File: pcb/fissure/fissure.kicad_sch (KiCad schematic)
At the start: 64 parts, among them J1 Conn_01x04_Female, J2 USB_C_Receptacle_USB2.0, J3 Conn_01x06, J4 Conn_01x06, J5 OLED, J6 Conn_01x06, J7 Conn_01x06, K1 KEY, K10 KEY, K11 KEY, K12 KEY, K13 KEY, K14 KEY, K15 KEY, K16 KEY, K17 KEY, K18 KEY, K19 KEY, K2 KEY, K20 KEY, K3 KEY, K4 KEY, K5 KEY, K6 KEY, K7 KEY, K8 KEY, K9 KEY, Q1 AO3401A, Q2 AO3401A, SW1 SW_Push, SW2 SW_Push, SW3 SW_SPDT, SW4 SW_SPDT, U1 Holyiot_18010, U2 MT25QL128ABA1ESE, U3 LTC4054ES5-4.2, U4 MCP1700-3302E_SOT23

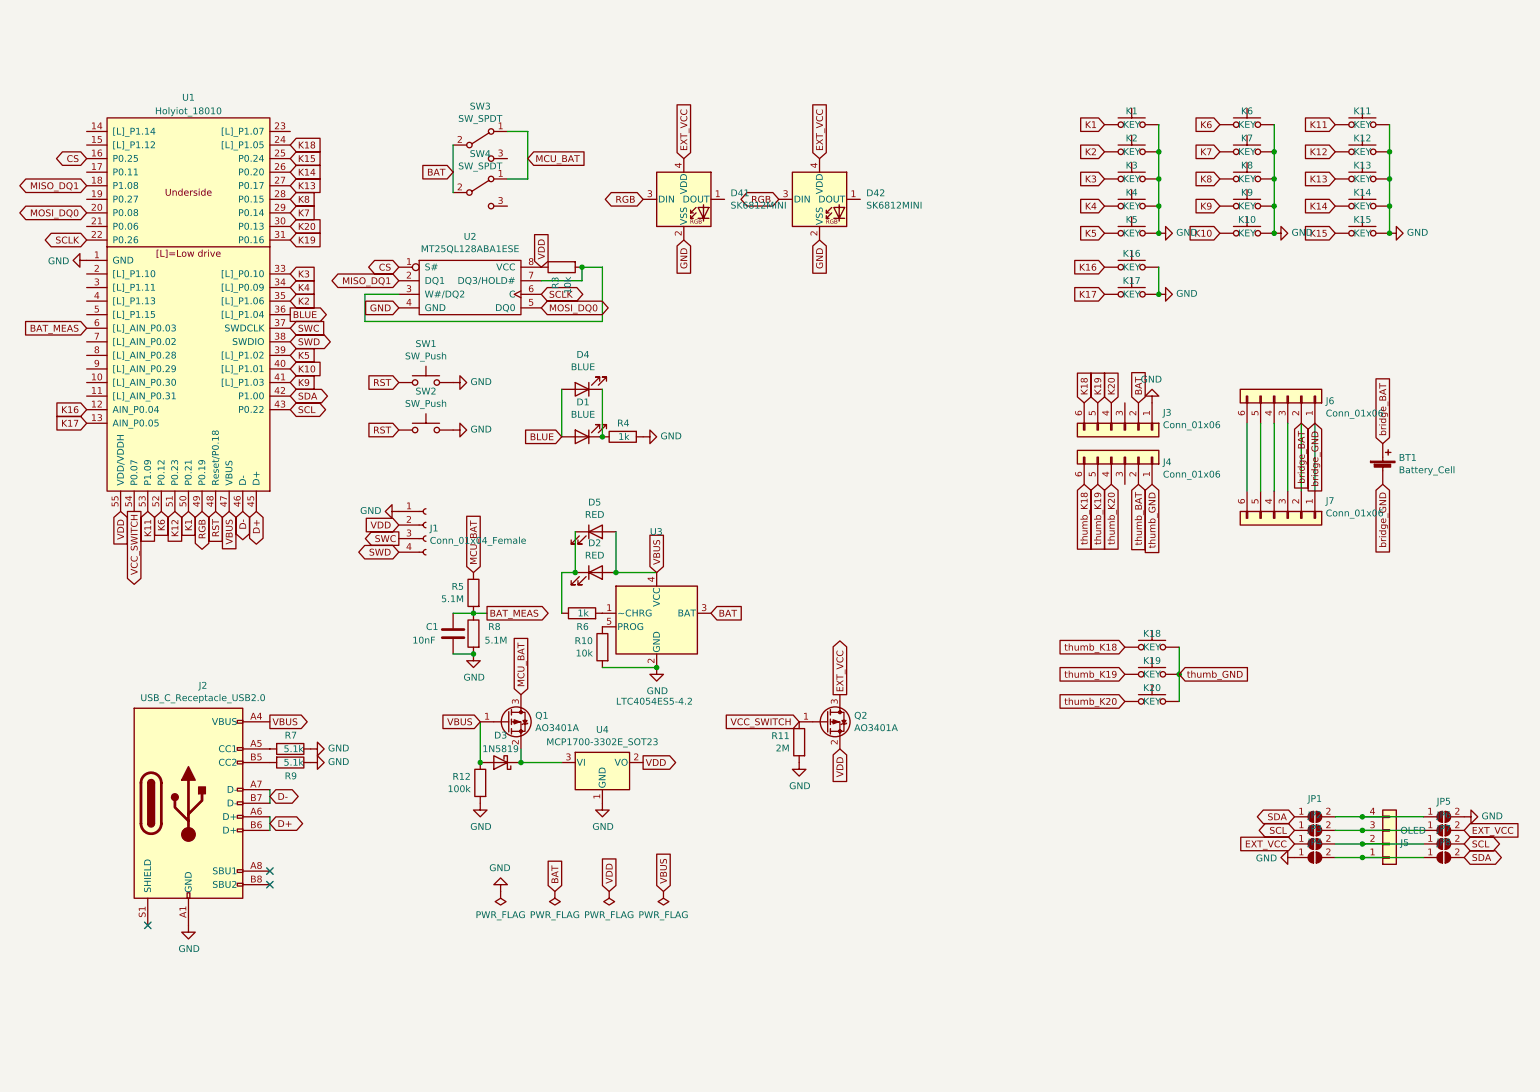
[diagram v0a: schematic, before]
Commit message: stagger update
- middle 2 mm up
- outer index flat with home
- narrower pinky columns
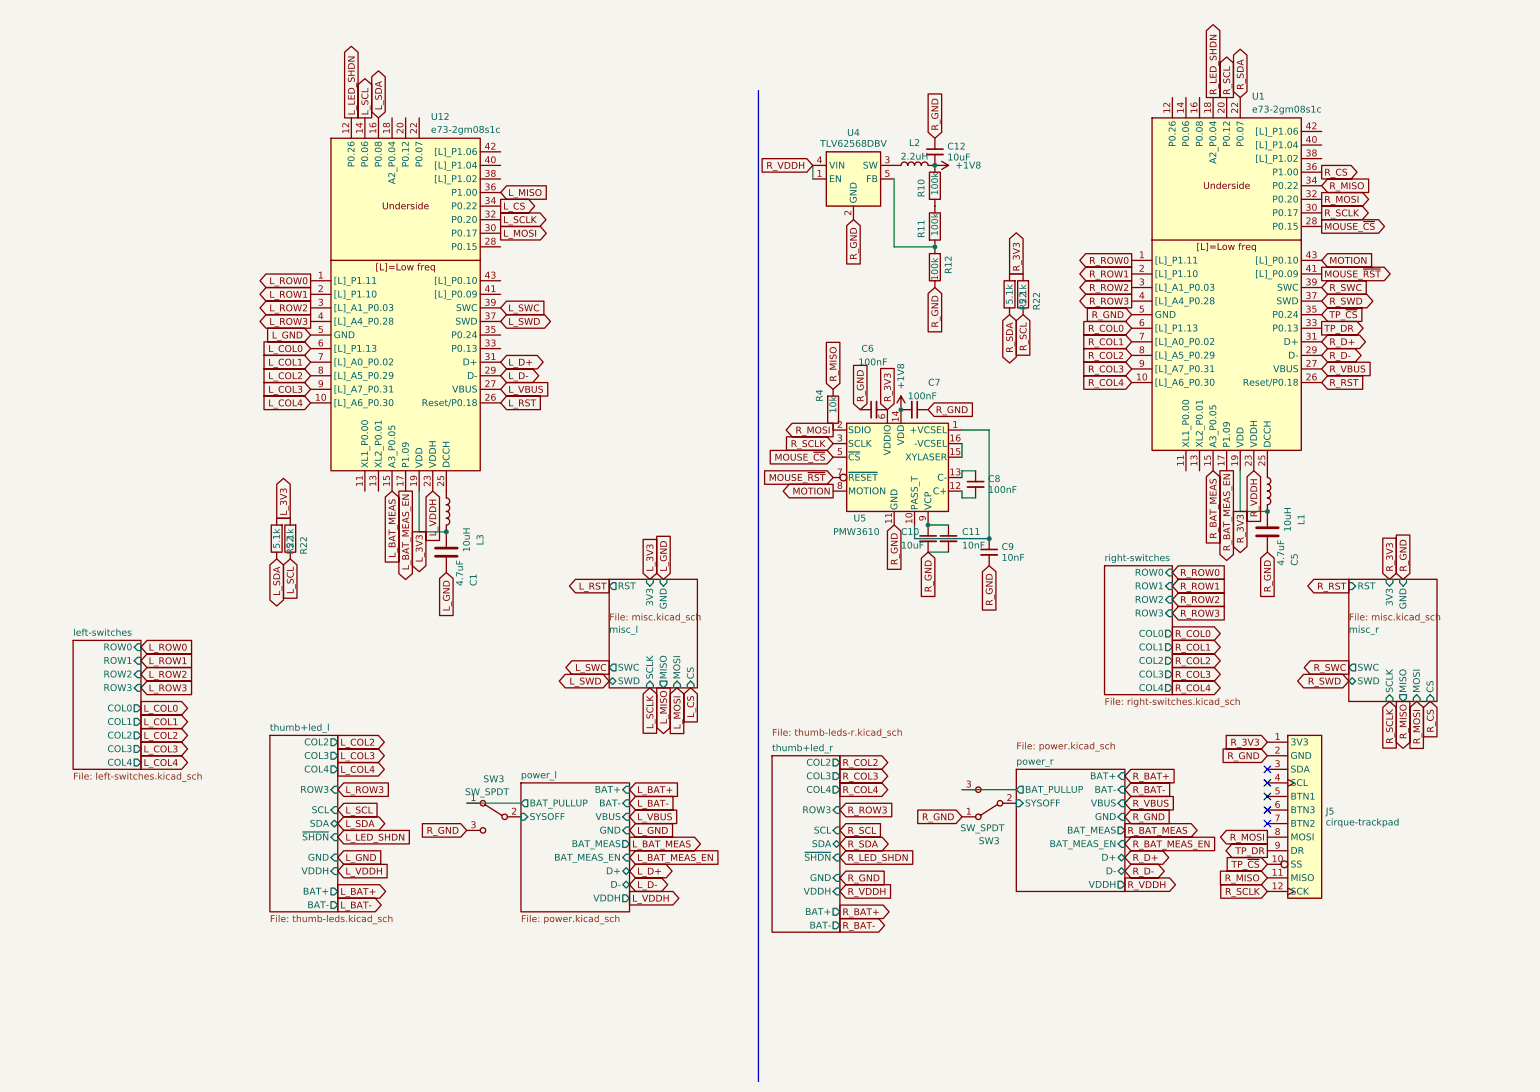
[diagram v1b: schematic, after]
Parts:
- removed BT1: Battery_Cell, misc:BA1AAAPC, symbol Device:Battery_Cell
- removed D1, D4: BLUE, LED_SMD:LED_1206_3216Metric, symbol Device:LED
- removed D2, D5: RED, LED_SMD:LED_1206_3216Metric, symbol Device:LED
- removed D3: 1N5819, Diode_SMD:D_SOD-323, symbol Diode:1N5819
- removed D41, D42: SK6812MINI, LED_SMD:LED_SK6812MINI_PLCC4_3.5x3.5mm_P1.75mm, symbol LED:SK6812MINI
- removed J1: Conn_01x04_Female, fissure:debug-port, symbol Connector:Conn_01x04_Female
- removed J2: USB_C_Receptacle_USB2.0, Connector_USB:USB_C_Receptacle_HRO_TYPE-C-31-M-12, symbol Connector:USB_C_Receptacle_USB2.0
- removed J3, J4: Conn_01x06, fissure:bridge-conn, symbol Connector_Generic:Conn_01x06
- removed J5: OLED, misc:OLED, symbol Connector_Generic:Conn_01x04
- removed J6, J7: Conn_01x06, fissure:bridge, symbol Connector_Generic:Conn_01x06
- removed JP1, JP2, JP3, JP4, JP5, JP6, JP7, JP8: SolderJumper_2_Open, Jumper:SolderJumper-2_P1.3mm_Open_RoundedPad1.0x1.5mm, symbol Jumper:SolderJumper_2_Open
- removed K1, K11, K12, K13, K16, K17, K18, K19, K2, K20, K3, K6, K7, K8: KEY, pg1350:PG1350-reversible-no-diode-short, symbol Switch:SW_Push
- removed K10, K15, K5: KEY, pg1350:PG1350-reversible-no-diode-short-offcenter-outer, symbol Switch:SW_Push
- removed K14, K4, K9: KEY, pg1350:PG1350-reversible-no-diode-short-offcenter, symbol Switch:SW_Push
- removed Q1, Q2: AO3401A, Package_TO_SOT_SMD:SOT-23, symbol Transistor_FET:AO3401A
- removed R3: 10k, Resistor_SMD:R_0805_2012Metric, symbol Device:R
- removed R5, R8: 5.1M, Resistor_SMD:R_0603_1608Metric, symbol Device:R
- removed R6: 1k, Resistor_SMD:R_0603_1608Metric, symbol Device:R
- removed R7, R9: 5.1k, Resistor_SMD:R_0603_1608Metric, symbol Device:R
- removed SW1, SW2: SW_Push, Button_Switch_SMD:SW_SPST_B3U-1000P, symbol Switch:SW_Push
- removed SW3, SW4: SW_SPDT, Button_Switch_SMD:SW_SPDT_PCM12, symbol Switch:SW_SPDT
- removed U1: Holyiot_18010, misc:Holyiot_18010, symbol holyiot_18010:Holyiot_18010
- removed U2: MT25QL128ABA1ESE, Package_SO:SOP-8_5.28x5.23mm_P1.27mm, symbol steno:MT25QL128ABA1ESE
- removed U3: LTC4054ES5-4.2, Package_TO_SOT_SMD:TSOT-23-5, symbol Battery_Management:LTC4054ES5-4.2
- removed U4: MCP1700-3302E_SOT23, Package_TO_SOT_SMD:SOT-23, symbol Regulator_Linear:MCP1700-3302E_SOT23
- added C10, C12: 10uF, Capacitor_SMD:C_0603_1608Metric, symbol Device:C_Small
- added C11, C9: 10nF, Capacitor_SMD:C_0603_1608Metric, symbol Device:C_Small
- added C5: 4.7uF, Capacitor_SMD:C_0603_1608Metric, symbol Device:C
- added C6, C7, C8: 100nF, Capacitor_SMD:C_0603_1608Metric, symbol Device:C_Small
- added J5: cirque-trackpad, Connector_FFC-FPC:Hirose_FH12-12S-0.5SH_1x12-1MP_P0.50mm_Horizontal, symbol misc:cirque-trackpad
- added L1, L3: 10uH, Inductor_SMD:L_0603_1608Metric, symbol Device:L
- added L2: 2.2uH, Inductor_SMD:L_1008_2520Metric, symbol Device:L
- added R22 (x4): 5.1k, Resistor_SMD:R_0603_1608Metric, symbol Device:R
- added SW3 (x2): SW_SPDT, Button_Switch_SMD:SW_SPDT_PCM12, symbol Switch:SW_SPDT
- added U1, U12: e73-2gm08s1c, mcu:e73-2g4m08s1c-shrunk, symbol mcu:e73-2gm08s1c
- added U4: TLV62568DBV, Package_TO_SOT_SMD:SOT-23-5, symbol Regulator_Switching:TLV62568DBV
- added U5: PMW3610, sensor:PMW3610, symbol sensor:PMW3610
- C1: value 10nF -> 4.7uF
- R10: value 10k -> 100k
- R11: value 2M -> 100k
- R4: value 1k -> 10k
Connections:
- net VBUS is gone; now on net GND: R12.1
- net GND: now also C10.2, C11.2, C12.1, C5.2, C6.1, C7.1, C9.2, J5.2 (GND), SW3.1 (A), SW3.3 (C), U1.21 (GND), U1.24 (GND), U1.5 (GND), U12.21 (GND), U12.24 (GND), U12.5 (GND), U4.2 (GND), U5.11 (GND); no longer R10.2, R11.2, R12.2, R4.2
- net R_MOSI: now reaches R4.1
- net R_MOSI: now also J5.8 (MOSI), U1.32 (P0.20), U5.2 (SDIO)
- net +1V8: now reaches R10.1
- net +1V8: now also C12.2, C7.2, L2.2, U5.14 (VDD)
- net BAT_MEAS renamed L_3V3
- net L_3V3: now also L3.2, R22.2, R22.2, U12.19 (VDD)
- net VCC_SWITCH: no longer names the net of R11.1
- net VCC_SWITCH: now also R10.2
- new net: L1.1, U1.25 (DCCH)
- new net: R11.2, R12.2, U4.5 (FB)
- new net: L3.1, U12.25 (DCCH)
- new net: C10.1, C11.1, U5.9 (VCP)
- new net: C9.1, U5.1 (+VCSEL), U5.10 (PASS_T)
- new net: C8.2, U5.12 (C+)
- new net: C8.1, U5.13 (C-)
- new net: U5.15 (XYLASER), U5.16 (-VCSEL)
- new net: L2.1, U4.3 (SW)
- new net L_BAT_MEAS: U12.15 (A3_P0.05)
- new net L_BAT_MEAS_EN: U12.17 (P1.09)
- new net L_COL0: U12.6 ([L]_P1.13)
- new net L_COL1: U12.7 ([L]_A0_P0.02)
- new net L_COL2: U12.8 ([L]_A5_P0.29)
- new net L_COL3: U12.9 ([L]_A7_P0.31)
- new net L_COL4: U12.10 ([L]_A6_P0.30)
- new net L_CS: U12.34 (P0.22)
- new net L_D+: U12.31 (D+)
- new net L_D-: U12.29 (D-)
- new net L_LED_SHDN: U12.12 (P0.26)
- new net L_MISO: U12.36 (P1.00)
- new net L_MOSI: U12.30 (P0.17)
- new net L_ROW0: U12.1 ([L]_P1.11)
- new net L_ROW1: U12.2 ([L]_P1.10)
- new net L_ROW2: U12.3 ([L]_A1_P0.03)
- new net L_ROW3: U12.4 ([L]_A4_P0.28)
- new net L_RST: U12.26 (Reset/P0.18)
- new net L_SCL: R22.1, U12.14 (P0.06)
- new net L_SCLK: U12.32 (P0.20)
- new net L_SDA: R22.1, U12.16 (P0.08)
- new net L_SWC: U12.39 (SWC)
- new net L_SWD: U12.37 (SWD)
- new net L_VBUS: U12.27 (VBUS)
- new net L_VDDH: U12.23 (VDDH)
- new net MOTION: U1.43 ([L]_P0.10), U5.8 (MOTION)
- new net MOUSE_~{CS}: U1.28 (P0.15), U5.5 (~{CS})
- new net MOUSE_~{RST}: U1.41 ([L]_P0.09), U5.7 (~{RESET})
- new net R_3V3: C5.1, C6.2, J5.1 (3V3), L1.2, R22.2, R22.2, U1.19 (VDD), U5.6 (VDDIO)
- new net R_BAT_MEAS: U1.15 (A3_P0.05)
- new net R_BAT_MEAS_EN: U1.17 (P1.09)
- new net R_COL0: U1.6 ([L]_P1.13)
- new net R_COL1: U1.7 ([L]_A0_P0.02)
- new net R_COL2: U1.8 ([L]_A5_P0.29)
- new net R_COL3: U1.9 ([L]_A7_P0.31)
- new net R_COL4: U1.10 ([L]_A6_P0.30)
- new net R_CS: U1.36 (P1.00)
- new net R_D+: U1.31 (D+)
- new net R_D-: U1.29 (D-)
- new net R_LED_SHDN: U1.18 (A2_P0.04)
- new net R_MISO: J5.11 (MISO), R4.2, U1.34 (P0.22)
- new net R_ROW0: U1.1 ([L]_P1.11)
- new net R_ROW1: U1.2 ([L]_P1.10)
- new net R_ROW2: U1.3 ([L]_A1_P0.03)
- new net R_ROW3: U1.4 ([L]_A4_P0.28)
- new net R_RST: U1.26 (Reset/P0.18)
- new net R_SCL: R22.1, U1.20 (P0.12)
- new net R_SCLK: J5.12 (SCK), U1.30 (P0.17), U5.3 (SCLK)
- new net R_SDA: R22.1, U1.22 (P0.07)
- new net R_SWC: U1.39 (SWC)
- new net R_SWD: U1.37 (SWD)
- new net R_VBUS: U1.27 (VBUS)
- new net R_VDDH: U1.23 (VDDH), U4.1 (EN), U4.4 (VIN)
- new net TP_DR: J5.9 (DR), U1.33 (P0.13)
- new net TP_~{CS}: J5.10 (SS), U1.35 (P0.24)
- new net power_l/BAT_PULLUP: SW3.1 (A)
- new net power_l/SYSOFF: SW3.2 (B)
- new net power_r/BAT_PULLUP: SW3.3 (C)
- new net power_r/SYSOFF: SW3.2 (B)
- no-connect marks 3 -> 5
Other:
- added sheet left-switches (left-switches.kicad_sch)
- added sheet misc_l (misc.kicad_sch)
- added sheet misc_r (misc.kicad_sch)
- added sheet power_l (power.kicad_sch)
- added sheet power_r (power.kicad_sch)
- added sheet right-switches (right-switches.kicad_sch)
- added sheet thumb+led_l (thumb-leds.kicad_sch)
- added sheet thumb+led_r (thumb-leds-r.kicad_sch)

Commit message: break out points
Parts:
- added TP1: CS, TestPoint:TestPoint_THTPad_D1.0mm_Drill0.5mm, symbol Connector:TestPoint_Small
- added TP2: SCLK, TestPoint:TestPoint_THTPad_D1.0mm_Drill0.5mm, symbol Connector:TestPoint_Small
- added TP3: MISO, TestPoint:TestPoint_THTPad_D1.0mm_Drill0.5mm, symbol Connector:TestPoint_Small
- added TP4: MOSI, TestPoint:TestPoint_THTPad_D1.0mm_Drill0.5mm, symbol Connector:TestPoint_Small
- added TP5: SDA, TestPoint:TestPoint_THTPad_D1.0mm_Drill0.5mm, symbol Connector:TestPoint_Small
- added TP6: SCL, TestPoint:TestPoint_THTPad_D1.0mm_Drill0.5mm, symbol Connector:TestPoint_Small
- added TP7: 3V3, TestPoint:TestPoint_THTPad_D1.0mm_Drill0.5mm, symbol Connector:TestPoint_Small
- added TP8: GND, TestPoint:TestPoint_THTPad_D1.0mm_Drill0.5mm, symbol Connector:TestPoint_Small
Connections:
- net GND: now also TP8.1
- net R_3V3: now also TP7.1
- net R_MISO: now also TP3.1
- net R_MOSI: now also TP4.1
- net R_SCL: now also TP6.1
- net R_SCLK: now also TP2.1
- net R_SDA: now also TP5.1
- net R_CS3: now reaches U1.16 (P0.08)
- net R_CS3: now also TP1.1
